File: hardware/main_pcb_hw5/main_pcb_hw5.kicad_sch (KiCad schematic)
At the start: 24 parts, among them J1 MEGA TOP, J2 MEGA BOTTOM, J3 CART SLOT TOP ROW, J4 CART SLOT BOTTOM ROW, J5 MEGA SIDE, J6 5V USB, J7 Conn_01x07, J8 EXP2, J9 EXP1, M2_3 Screw_Terminal_01x01, M2_4 Screw_Terminal_01x01, M2_5 Screw_Terminal_01x01, M2_6 Screw_Terminal_01x01, M2_7 Screw_Terminal_01x01, M2_8 Screw_Terminal_01x01, M2_9 Screw_Terminal_01x01, SW1 VOLTAGE, SW2 POWER

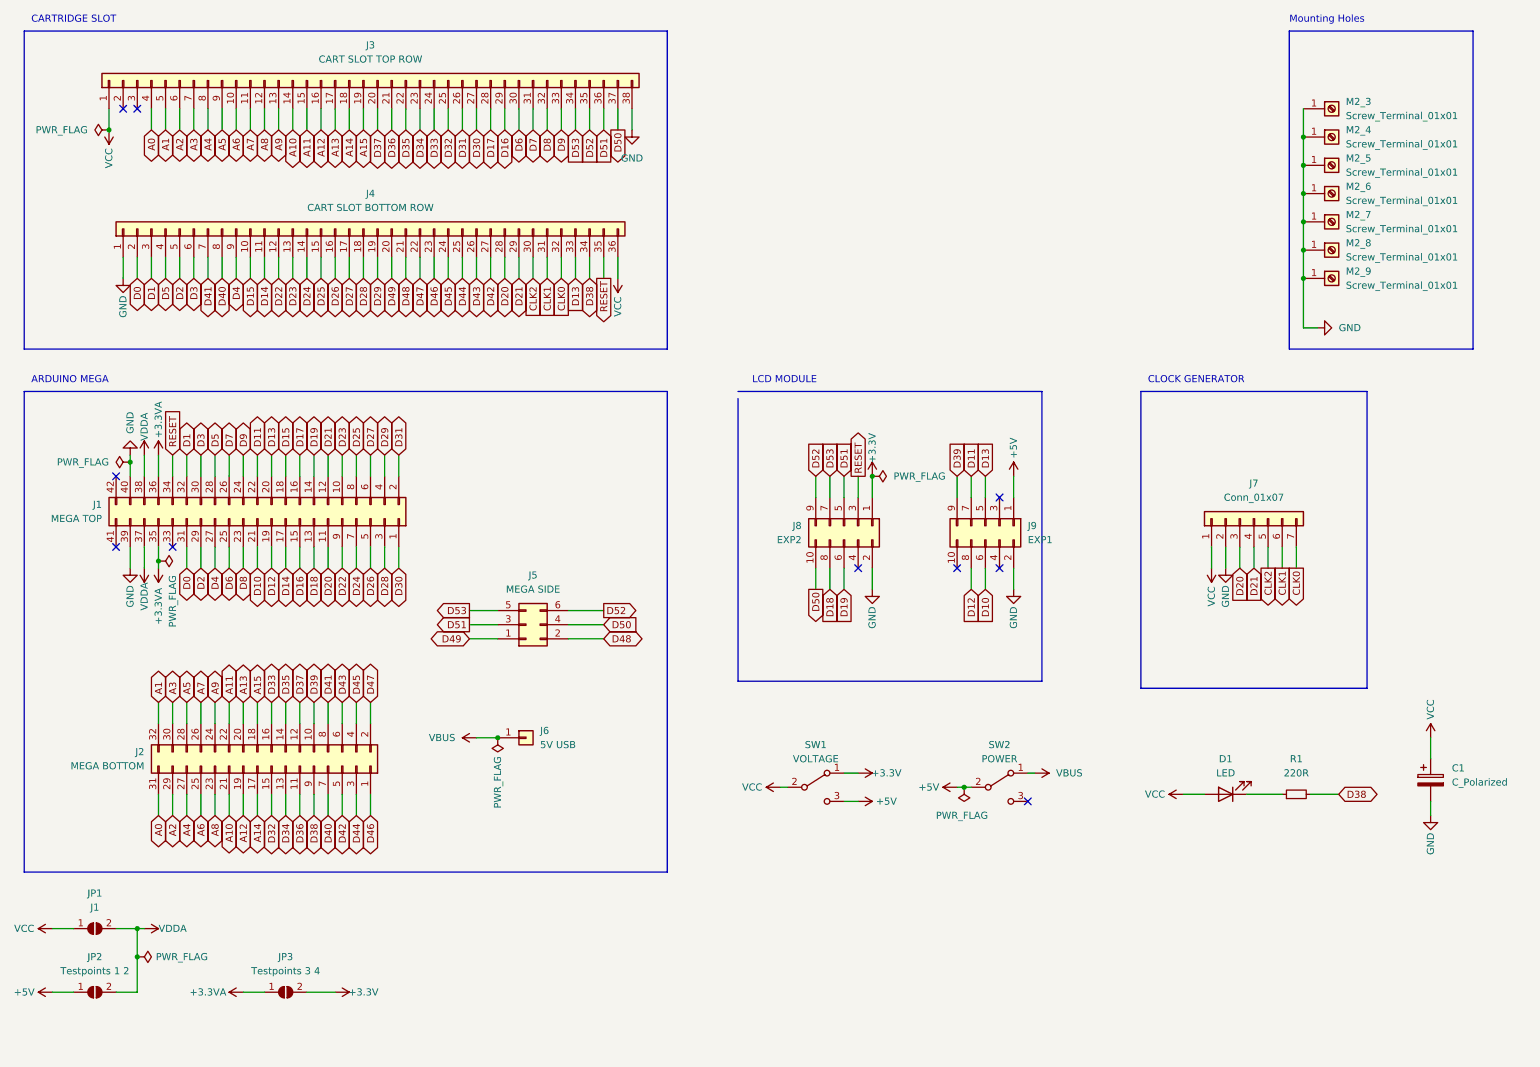
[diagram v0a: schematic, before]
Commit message: Change MCU module on schematic
Replace Mega embed with standard Mega R3.
Added 2 voltage regulators to main pcb.
-moved voltage selection to daughterboard (remove main switch)
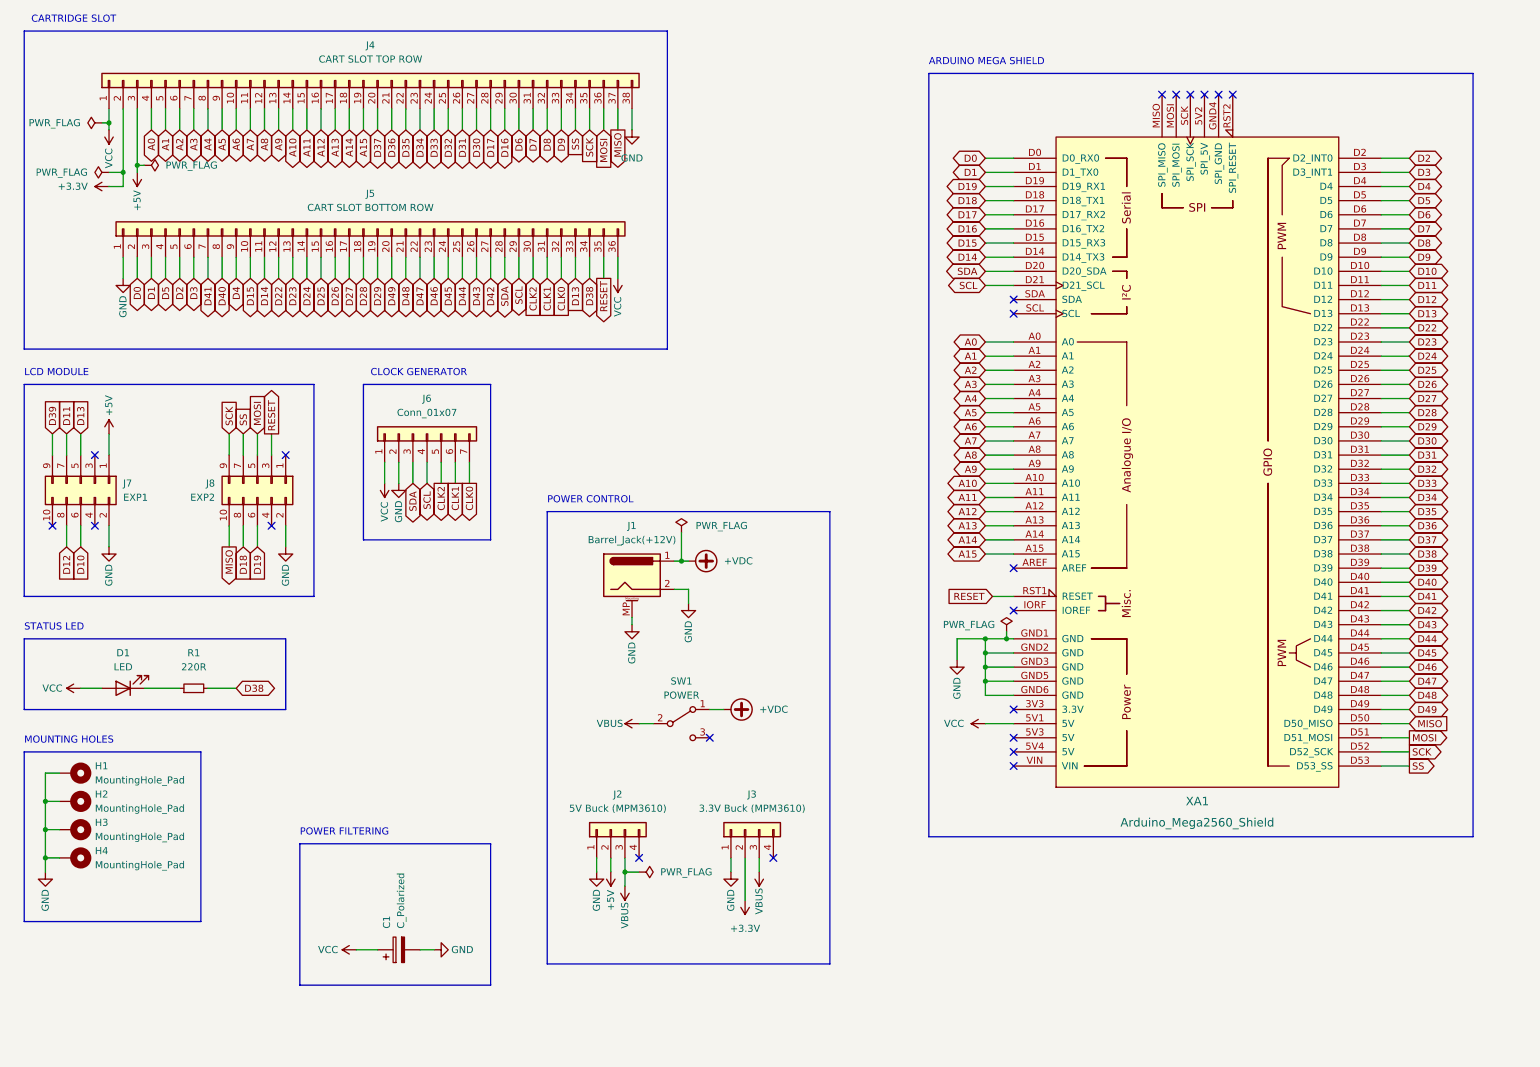
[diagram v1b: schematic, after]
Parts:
- removed J1: MEGA TOP, Connector_PinSocket_2.54mm:PinSocket_2x21_P2.54mm_Vertical, symbol Connector_Generic:Conn_02x21_Odd_Even
- removed J2: MEGA BOTTOM, Connector_PinSocket_2.54mm:PinSocket_2x16_P2.54mm_Vertical, symbol Connector_Generic:Conn_02x16_Odd_Even
- removed J5: MEGA SIDE, Connector_PinSocket_2.54mm:PinSocket_2x03_P2.54mm_Vertical, symbol Connector_Generic:Conn_02x03_Odd_Even
- removed J6: 5V USB, Connector_PinHeader_2.54mm:PinHeader_1x01_P2.54mm_Vertical, symbol Connector_Generic:Conn_01x01
- removed JP1: J1, Jumper:SolderJumper-2_P1.3mm_Open_Pad1.0x1.5mm, symbol Jumper:SolderJumper_2_Open
- removed JP2: Testpoints 1 2, Jumper:SolderJumper-2_P1.3mm_Open_Pad1.0x1.5mm, symbol Jumper:SolderJumper_2_Open
- removed JP3: Testpoints 3 4, Jumper:SolderJumper-2_P1.3mm_Open_Pad1.0x1.5mm, symbol Jumper:SolderJumper_2_Open
- removed M2_3, M2_4, M2_5, M2_6, M2_7, M2_8, M2_9: Screw_Terminal_01x01, MountingHole:MountingHole_2.2mm_M2_ISO7380_Pad, symbol Connector:Screw_Terminal_01x01
- removed SW1: VOLTAGE, Button_Switch_THT:SW_CuK_OS102011MA1QN1_SPDT_Angled, symbol Switch:SW_SPDT
- added H1, H2, H3, H4: MountingHole_Pad, MountingHole:MountingHole_3.2mm_M3_Pad, symbol Mechanical:MountingHole_Pad
- added J1: Barrel_Jack(+12V), Connector_BarrelJack:BarrelJack_Horizontal, symbol Connector:Barrel_Jack_MountingPin
- added J2: 5V Buck (MPM3610), Connector_PinHeader_2.54mm:PinHeader_1x04_P2.54mm_Vertical, symbol Connector_Generic:Conn_01x04
- added J3: 3.3V Buck (MPM3610), Connector_PinHeader_2.54mm:PinHeader_1x04_P2.54mm_Vertical, symbol Connector_Generic:Conn_01x04
- added XA1: Arduino_Mega2560_Shield, Arduino_Library:Arduino_Mega2560_Shield, symbol arduino_boards_library:Arduino_Mega2560_Shield
- renumbered J3 to J4, J4 to J5, J7 to J6, J9 to J7, SW2 to SW1
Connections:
- net +5V: now also J4.3 (Pin_3), J2.2 (Pin_2); no longer SW1.2 (B)
- net A0: now also XA1.A0
- net A1: now also XA1.A1
- net A10: now also XA1.A10
- net A11: now also XA1.A11
- net A12: now also XA1.A12
- net A13: now also XA1.A13
- net A14: now also XA1.A14
- net A15: now also XA1.A15
- net A2: now also XA1.A2
- net A3: now also XA1.A3
- net A4: now also XA1.A4
- net A5: now also XA1.A5
- net A6: now also XA1.A6
- net A7: now also XA1.A7
- net A8: now also XA1.A8
- net A9: now also XA1.A9
- net D0: now also XA1.D0 (D0_RX0)
- net D1: now also XA1.D1 (D1_TX0)
- net D10: now also XA1.D10
- net D11: now also XA1.D11
- net D12: now also XA1.D12
- net D13: now also XA1.D13
- net D14: now also XA1.D14 (D14_TX3)
- net D15: now also XA1.D15 (D15_RX3)
- net D16: now also XA1.D16 (D16_TX2)
- net D17: now also XA1.D17 (D17_RX2)
- net D18: now also XA1.D18 (D18_TX1)
- net D19: now also XA1.D19 (D19_RX1)
- net D2: now also XA1.D2 (D2_INT0)
- net D22: now also XA1.D22
- net D23: now also XA1.D23
- net D24: now also XA1.D24
- net D25: now also XA1.D25
- net D26: now also XA1.D26
- net D27: now also XA1.D27
- net D28: now also XA1.D28
- net D29: now also XA1.D29
- net D3: now also XA1.D3 (D3_INT1)
- net D30: now also XA1.D30
- net D31: now also XA1.D31
- net D32: now also XA1.D32
- net D33: now also XA1.D33
- net D34: now also XA1.D34
- net D35: now also XA1.D35
- net D36: now also XA1.D36
- net D37: now also XA1.D37
- net D38: now also XA1.D38
- net D39: now also XA1.D39
- net D4: now also XA1.D4
- net D40: now also XA1.D40
- net D41: now also XA1.D41
- net D42: now also XA1.D42
- net D43: now also XA1.D43
- net D44: now also XA1.D44
- net D45: now also XA1.D45
- net D46: now also XA1.D46
- net D47: now also XA1.D47
- net D48: now also XA1.D48
- net D49: now also XA1.D49
- net D5: now also XA1.D5
- net D6: now also XA1.D6
- net D7: now also XA1.D7
- net D8: now also XA1.D8
- net D9: now also XA1.D9
- net GND: now also H1.1, H2.1, H3.1, H4.1, J1.2, J1.MP (MountPin), J2.1 (Pin_1), J3.1 (Pin_1), XA1.GND1 (GND), XA1.GND2 (GND), XA1.GND3 (GND), XA1.GND5 (GND), XA1.GND6 (GND)
- net RESET: now also XA1.RST1 (RESET)
- net VBUS: now also SW1.2 (B), J2.3 (Pin_3), J3.3 (Pin_3); no longer SW1.1 (A)
- net VCC: now also XA1.5V1 (5V)
- net +3.3V: now reaches J4.2 (Pin_2)
- net +3.3V: now also J3.2 (Pin_2)
- net +3V3: no longer names the net of J8.1 (Pin_1)
- net D20 renamed SDA
- net SDA: now also XA1.D20 (D20_SDA)
- net D21 renamed SCL
- net SCL: now also XA1.D21 (D21_SCL)
- net D50 renamed MISO
- net MISO: now also XA1.D50 (D50_MISO)
- net D51 renamed MOSI
- net MOSI: now also XA1.D51 (D51_MOSI)
- net D52 renamed SCK
- net SCK: now also XA1.D52 (D52_SCK)
- net D53 renamed SS
- net SS: now also XA1.D53 (D53_SS)
- new net +VDC: J1.1, SW1.1 (A)
- no-connect marks 10 -> 22
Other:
- note added: "ARDUINO MEGA SHIELD"
- note added: "MOUNTING HOLES"
- note added: "POWER CONTROL"
- note added: "POWER FILTERING"
- note added: "STATUS LED"
- note removed: "ARDUINO MEGA"
- note removed: "Mounting Holes"
- moved on the sheet: C1, D1, J6, J7, J8, R1, SW1

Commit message: export schematic pdf
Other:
- title: OSCR HW5 -> OSCR Shield
- moved on the sheet: C1, J1, J2, J3, SW1, XA1

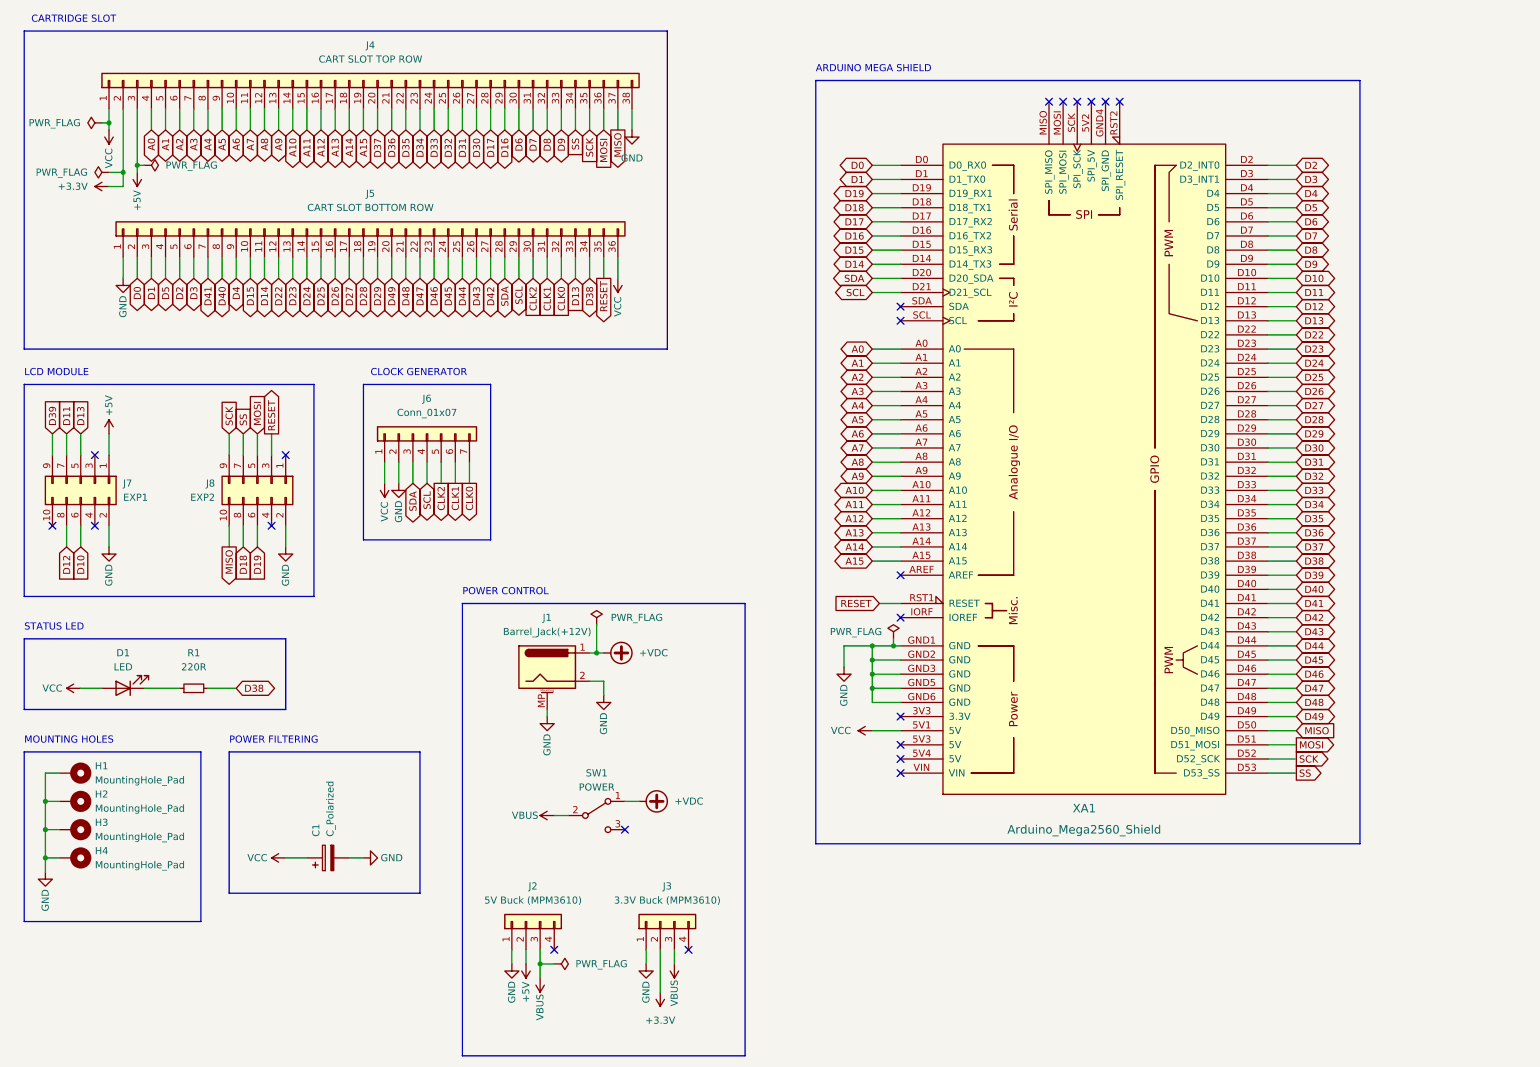
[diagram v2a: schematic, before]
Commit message: Update Main PCB
Change basic design to a shield. Remove GBA Port. Add buck converters to main board.
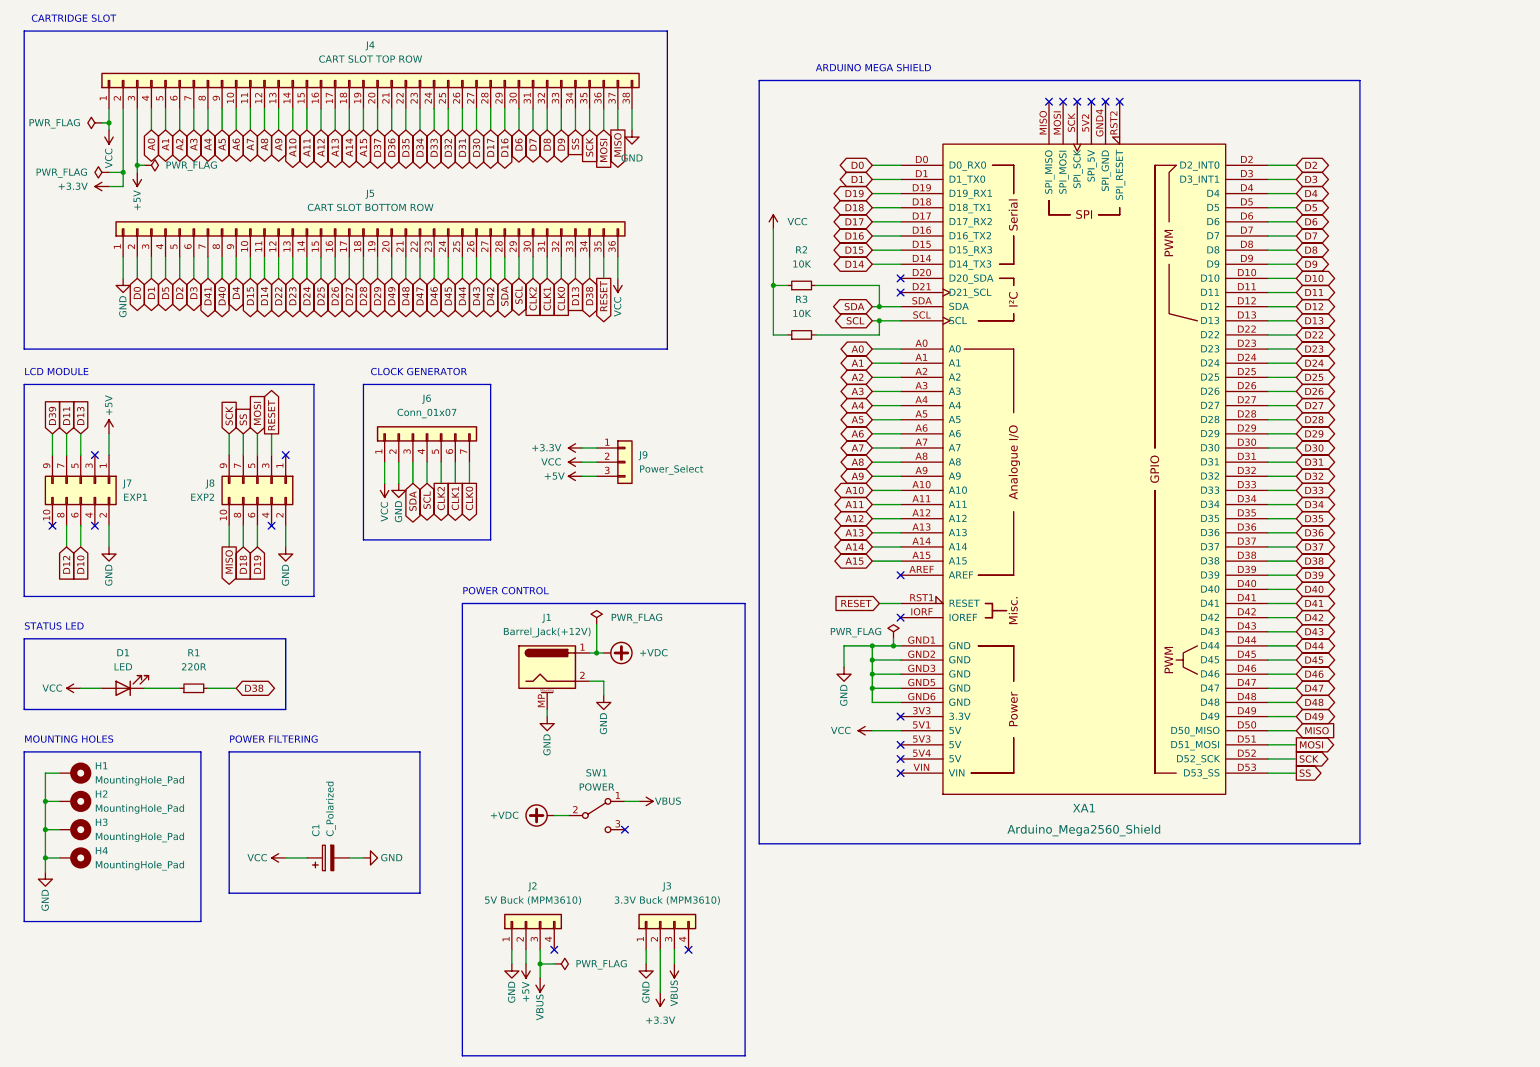
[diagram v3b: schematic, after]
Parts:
- removed XA1: Arduino_Mega2560_Shield, Arduino_Library:Arduino_Mega2560_Shield, symbol arduino_boards_library:Arduino_Mega2560_Shield
- added J9: Power_Select, Connector_PinHeader_2.54mm:PinHeader_1x03_P2.54mm_Vertical, symbol Connector_Generic:Conn_01x03
- added R2, R3: 10K, Resistor_THT:R_Axial_DIN0207_L6.3mm_D2.5mm_P7.62mm_Horizontal, symbol Device:R_Small
- added XA1: Arduino_Mega2560_Shield, Arduino:Arduino_Mega2560_Shield, symbol arduino:Arduino_Mega2560_Shield
- J6: footprint Connector_PinHeader_2.54mm:PinHeader_1x07_P2.54mm_Vertical -> Connector_PinSocket_2.54mm:PinSocket_1x07_P2.54mm_Vertical
- R1: footprint Resistor_THT:R_Axial_DIN0207_L6.3mm_D2.5mm_P10.16mm_Horizontal -> Resistor_THT:R_Axial_DIN0207_L6.3mm_D2.5mm_P7.62mm_Horizontal
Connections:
- net +3.3V: now also J9.1 (Pin_1)
- net +5V: now also J9.3 (Pin_3)
- net +VDC: now also SW1.2 (B); no longer SW1.1 (A)
- net A0: now also XA1.A0
- net A1: now also XA1.A1
- net A10: now also XA1.A10
- net A11: now also XA1.A11
- net A12: now also XA1.A12
- net A13: now also XA1.A13
- net A14: now also XA1.A14
- net A15: now also XA1.A15
- net A2: now also XA1.A2
- net A3: now also XA1.A3
- net A4: now also XA1.A4
- net A5: now also XA1.A5
- net A6: now also XA1.A6
- net A7: now also XA1.A7
- net A8: now also XA1.A8
- net A9: now also XA1.A9
- net D0: now also XA1.D0 (D0_RX0)
- net D1: now also XA1.D1 (D1_TX0)
- net D10: now also XA1.D10
- net D11: now also XA1.D11
- net D12: now also XA1.D12
- net D13: now also XA1.D13
- net D14: now also XA1.D14 (D14_TX3)
- net D15: now also XA1.D15 (D15_RX3)
- net D16: now also XA1.D16 (D16_TX2)
- net D17: now also XA1.D17 (D17_RX2)
- net D18: now also XA1.D18 (D18_TX1)
- net D19: now also XA1.D19 (D19_RX1)
- net D2: now also XA1.D2 (D2_INT0)
- net D22: now also XA1.D22
- net D23: now also XA1.D23
- net D24: now also XA1.D24
- net D25: now also XA1.D25
- net D26: now also XA1.D26
- net D27: now also XA1.D27
- net D28: now also XA1.D28
- net D29: now also XA1.D29
- net D3: now also XA1.D3 (D3_INT1)
- net D30: now also XA1.D30
- net D31: now also XA1.D31
- net D32: now also XA1.D32
- net D33: now also XA1.D33
- net D34: now also XA1.D34
- net D35: now also XA1.D35
- net D36: now also XA1.D36
- net D37: now also XA1.D37
- net D38: now also XA1.D38
- net D39: now also XA1.D39
- net D4: now also XA1.D4
- net D40: now also XA1.D40
- net D41: now also XA1.D41
- net D42: now also XA1.D42
- net D43: now also XA1.D43
- net D44: now also XA1.D44
- net D45: now also XA1.D45
- net D46: now also XA1.D46
- net D47: now also XA1.D47
- net D48: now also XA1.D48
- net D49: now also XA1.D49
- net D5: now also XA1.D5
- net D6: now also XA1.D6
- net D7: now also XA1.D7
- net D8: now also XA1.D8
- net D9: now also XA1.D9
- net GND: now also XA1.GND1 (GND), XA1.GND2 (GND), XA1.GND3 (GND), XA1.GND5 (GND), XA1.GND6 (GND)
- net MISO: now also XA1.D50 (D50_MISO)
- net MOSI: now also XA1.D51 (D51_MOSI)
- net RESET: now also XA1.RST1 (RESET)
- net SCK: now also XA1.D52 (D52_SCK)
- net SCL: now also R3.2, XA1.SCL
- net SDA: now also R2.2, XA1.SDA
- net SS: now also XA1.D53 (D53_SS)
- net VBUS: now also SW1.1 (A); no longer SW1.2 (B)
- net VCC: now also J9.2 (Pin_2), R2.1, R3.1, XA1.5V1 (5V)
